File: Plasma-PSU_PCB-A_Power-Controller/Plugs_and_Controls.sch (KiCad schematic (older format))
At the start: 31 parts, among them J201 PWR_FWD, J202 PWM_FWD, J203 Molex Mini-fit Jr. 39-28-1243, J204 Molex Mini-fit Jr. 39-28-1083, J205 Molex Mini-fit Jr. 39-28-1083, J206 Pinheader Controls, J207 ENBL_FWD, Q201 BC818, Q202 BC818, Q203 BT169B, Q204 BC808, U201 STM6600

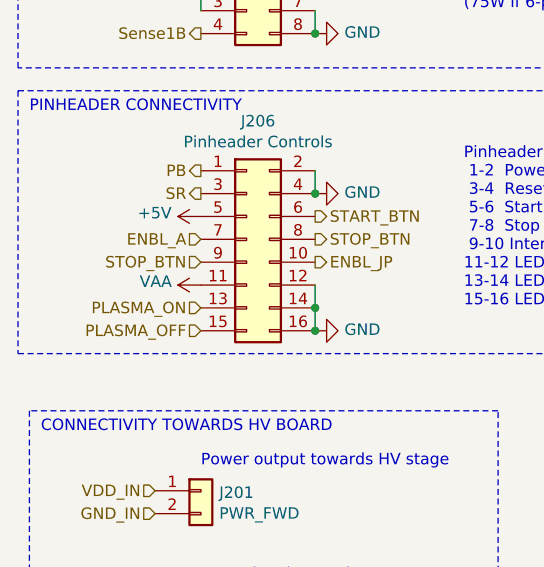
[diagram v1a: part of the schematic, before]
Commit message: FET & L revision w/ LTpowerCAD
LTpowerCAD tool used to revise selection of:
- main inductor
- control FET
- sync FET
- input and output capacitor banks
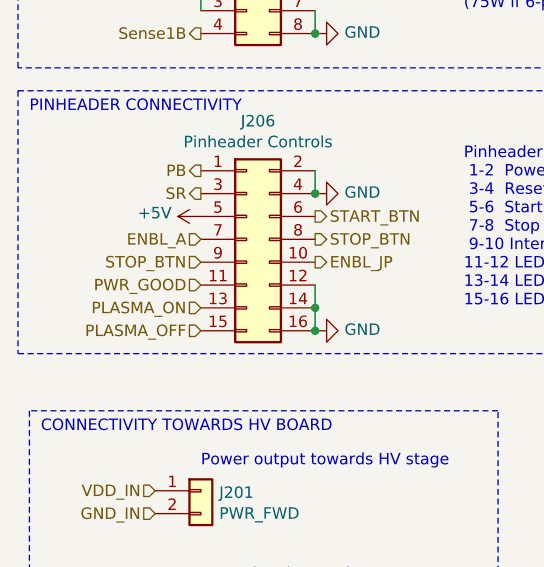
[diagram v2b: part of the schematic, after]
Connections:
- net VAA is gone; now on net PWR_GOOD: J206.11 (Pin_11)
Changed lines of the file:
@@
 Wire Wire Line
 	1900 1900 1900 1800
-$Comp
-L power:VAA #PWR0213
-U 1 1 5E9816A9
-P 1400 4600
-F 0 "#PWR0213" H 1400 4450 50  0001 C CNN
-F 1 "VAA" V 1415 4727 50  0000 L CNN
-F 2 "" H 1400 4600 50  0001 C CNN
-F 3 "" H 1400 4600 50  0001 C CNN
-	1    1400 4600
-	0    -1   -1   0
-$EndComp
 Wire Wire Line
 	1900 4800 1900 4700
@@
 Text HLabel 1400 1700 0    50   Output ~ 0
 PWR_GOOD
+Text HLabel 1400 4600 0    50   Input ~ 0
+PWR_GOOD
 $EndSCHEMATC
